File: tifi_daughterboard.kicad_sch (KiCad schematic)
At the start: 23 parts

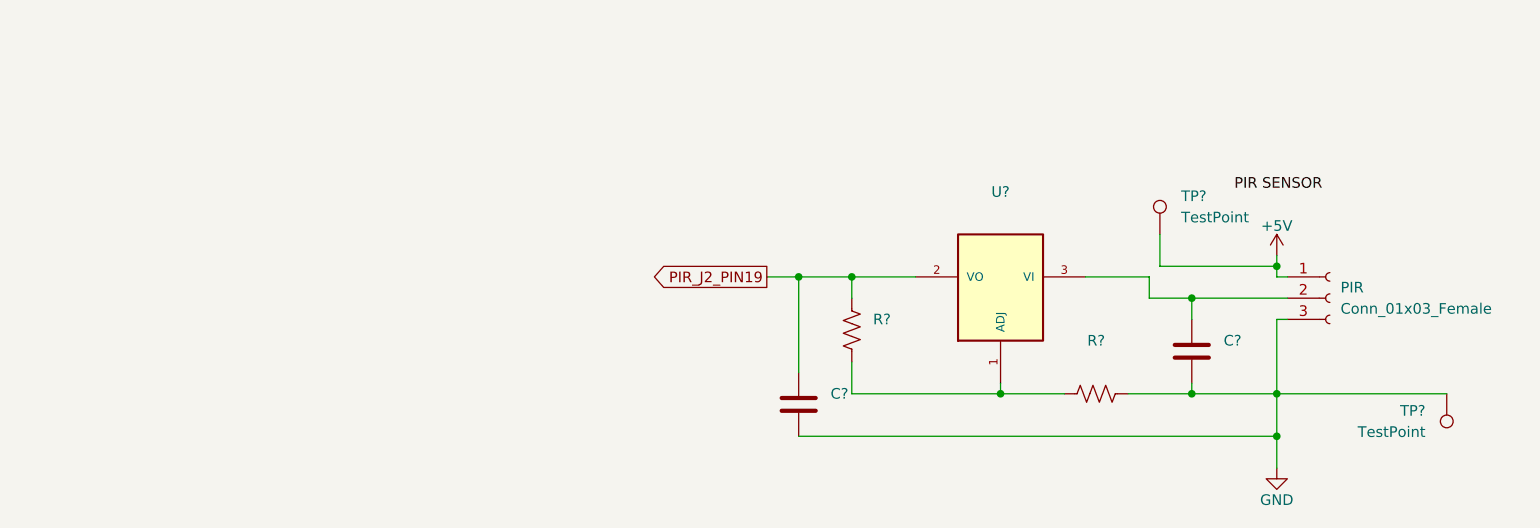
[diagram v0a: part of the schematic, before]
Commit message: Added JST connector for stemma
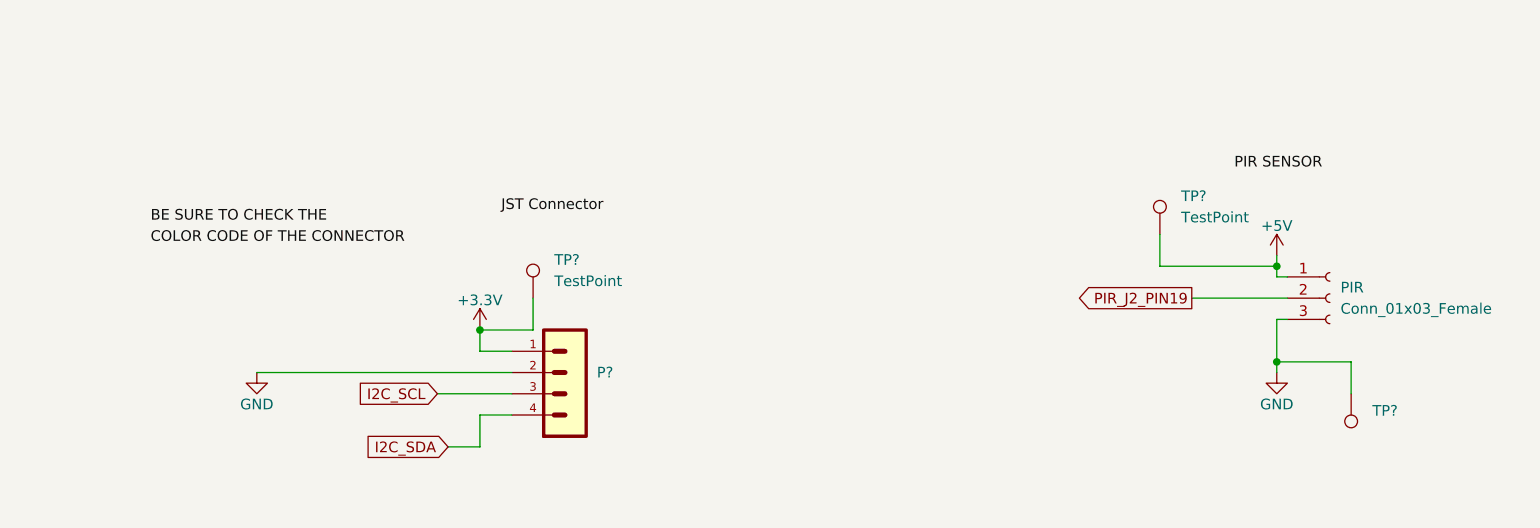
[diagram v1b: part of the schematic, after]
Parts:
- removed C? (x2): (no value), symbol Device:C
- removed R? (x2): (no value), symbol Device:R_US
- removed U?: (no value), symbol LM317:LM317
- added P?: (no value), symbol B4B-PH-K:B4B-PH-K
- added TP?: TestPoint, TestPoint:TestPoint_THTPad_1.0x1.0mm_Drill0.5mm, symbol Connector:TestPoint
- J? (x2): footprint (none) -> Connector_PinHeader_1.00mm:PinHeader_2x10_P1.00mm_Vertical
- LDR: footprint NSL_19M51 -> New Symbols:NSL_19M51
- PIR: footprint (none) -> Connector_PinHeader_1.00mm:PinHeader_1x03_P1.00mm_Vertical
- TP? (x7): footprint (none) -> TestPoint:TestPoint_THTPad_1.0x1.0mm_Drill0.5mm
- TP?: value TestPoint -> (none); footprint (none) -> TestPoint:TestPoint_THTPad_1.0x1.0mm_Drill0.5mm
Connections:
- net +3.3V: now also P?.1, TP?.1
- net GND: now also P?.2
- net I2C_SCL: now also P?.3
- net I2C_SDA: now also P?.4
- net PIR_J2_PIN19: now also PIR.2 (Pin_2)
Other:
- moved on the sheet: TP?

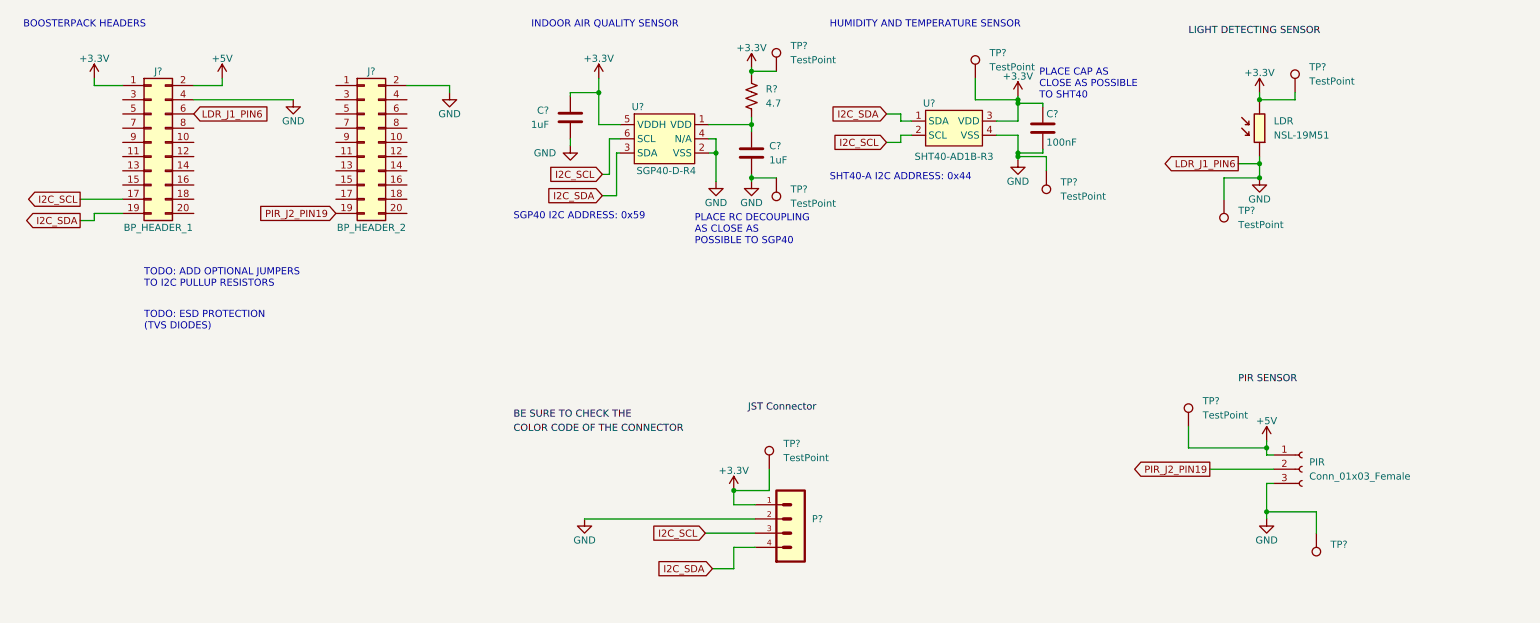
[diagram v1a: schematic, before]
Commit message: Change STEMMA QT connector.
The previous connector had 2mm pitch, changed to 1mm pitch.
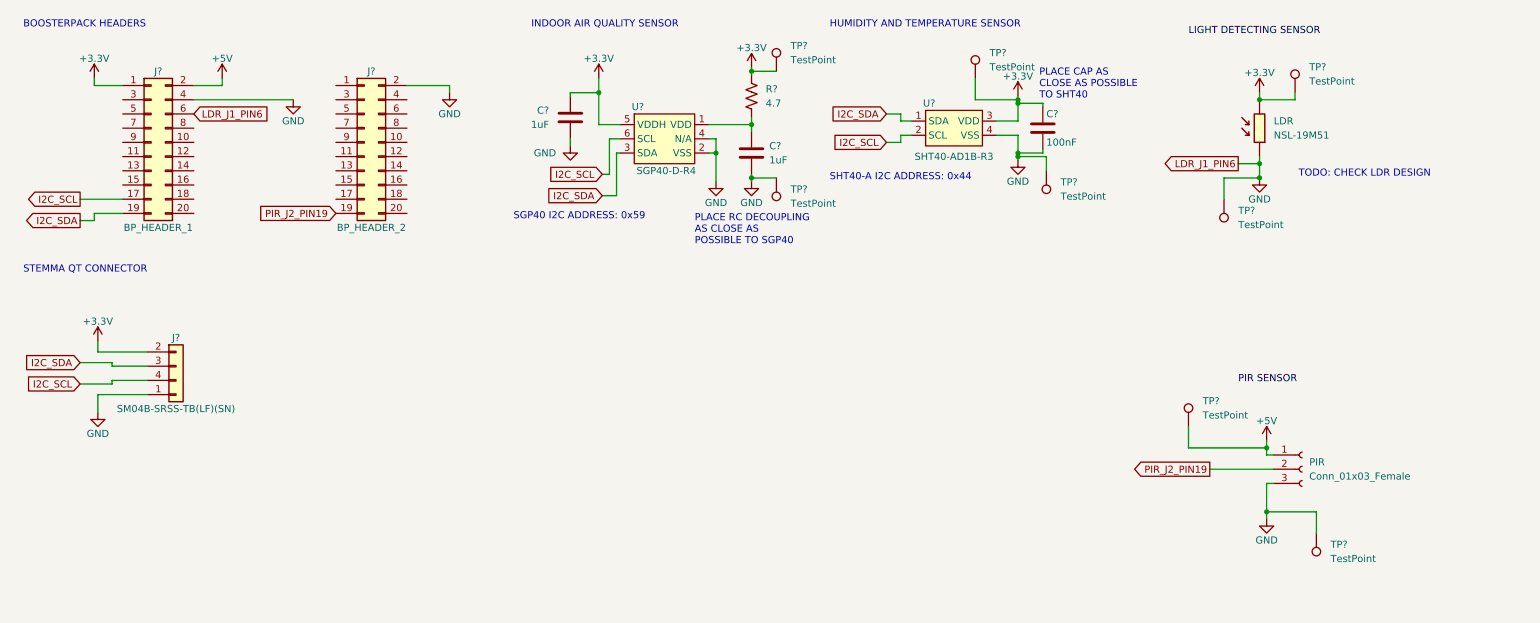
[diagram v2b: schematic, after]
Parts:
- removed P?: (no value), symbol B4B-PH-K:B4B-PH-K
- removed TP?: TestPoint, TestPoint:TestPoint_THTPad_1.0x1.0mm_Drill0.5mm, symbol Connector:TestPoint
- added J?: SM04B-SRSS-TB(LF)(SN), symbol Connector_Generic:Conn_01x04
- TP?: value (none) -> TestPoint
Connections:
- net +3.3V: now also J?.2 (Pin_2)
- net GND: now also J?.1 (Pin_1)
- net I2C_SCL: now also J?.4 (Pin_4)
- net I2C_SDA: now also J?.3 (Pin_3)
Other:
- note added: "STEMMA QT CONNECTOR"
- note added: "TODO: CHECK LDR DESIGN"
- note removed: "TODO: ADD OPTIONAL JUMPERS TO I2C PULLUP RESISTORS"
- note removed: "TODO: ESD PROTECTION (TVS DIODES)"

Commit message: Corrected pitch on BoosterPack headers footprint.
The previous pitch is 1mm, needed to be 2.54mm.
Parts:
- J? (x2): footprint Connector_PinHeader_1.00mm:PinHeader_2x10_P1.00mm_Vertical -> Connector_PinHeader_2.54mm:PinHeader_2x10_P2.54mm_Vertical
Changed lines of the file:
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@@
     (property "Reference" "J?" (id 0) (at 81.28 27.94 0))
     (property "Value" "BP_HEADER_2" (id 1) (at 81.28 55.88 0))
-    (property "Footprint" "Connector_PinHeader_1.00mm:PinHeader_2x10_P1.00mm_Vertical" (id 2) (at 80.01 40.64 0)
+    (property "Footprint" "Connector_PinHeader_2.54mm:PinHeader_2x10_P2.54mm_Vertical" (id 2) (at 80.01 40.64 0)
       (effects (font (size 1.27 1.27)) hide)
     )
@@
   (symbol (lib_id "power:+3.3V") (at 32.385 76.2 0) (unit 1)
     (in_bom yes) (on_board yes)
-    (property "Reference" "#PWR?" (id 0) (at 32.385 80.01 0)
+    (property "Reference" "#PWR0117" (id 0) (at 32.385 80.01 0)
       (effects (font (size 1.27 1.27)) hide)
     )
@@
     (property "Reference" "J?" (id 0) (at 43.18 27.94 0))
     (property "Value" "BP_HEADER_1" (id 1) (at 43.18 55.88 0))
-    (property "Footprint" "Connector_PinHeader_1.00mm:PinHeader_2x10_P1.00mm_Vertical" (id 2) (at 41.91 40.64 0)
+    (property "Footprint" "Connector_PinHeader_2.54mm:PinHeader_2x10_P2.54mm_Vertical" (id 2) (at 41.91 40.64 0)
       (effects (font (size 1.27 1.27)) hide)
     )
@@
   (symbol (lib_id "power:GND") (at 32.385 88.9 0) (unit 1)
     (in_bom yes) (on_board yes)
-    (property "Reference" "#PWR?" (id 0) (at 32.385 95.25 0)
+    (property "Reference" "#PWR0116" (id 0) (at 32.385 95.25 0)
       (effects (font (size 1.27 1.27)) hide)
     )
@@
       (reference "#PWR0115") (unit 1) (value "GND") (footprint "")
     )
+    (path "/fef7b405-bcca-4f18-8c18-a8e7a2c24140"
+      (reference "#PWR0116") (unit 1) (value "GND") (footprint "")
+    )
     (path "/5be1ee84-24e6-4a1e-a679-030b25f95ea3"
-      (reference "#PWR?") (unit 1) (value "+3.3V") (footprint "")
-    )
-    (path "/fef7b405-bcca-4f18-8c18-a8e7a2c24140"
-      (reference "#PWR?") (unit 1) (value "GND") (footprint "")
+      (reference "#PWR0117") (unit 1) (value "+3.3V") (footprint "")
     )
     (path "/2c04621a-bbf8-472b-bd15-1b74530f6f21"
@@
     )
     (path "/03e73a6c-6a66-4743-9386-abd83f09d2a2"
-      (reference "J?") (unit 1) (value "BP_HEADER_2") (footprint "Connector_PinHeader_1.00mm:PinHeader_2x10_P1.00mm_Vertical")
+      (reference "J?") (unit 1) (value "BP_HEADER_2") (footprint "Connector_PinHeader_2.54mm:PinHeader_2x10_P2.54mm_Vertical")
     )
     (path "/7b912d29-33dd-4ac7-bc62-fbbca0b985f1"
@@
     )
     (path "/eec51399-1c9c-497c-8d0a-e34cae999a37"
-      (reference "J?") (unit 1) (value "BP_HEADER_1") (footprint "Connector_PinHeader_1.00mm:PinHeader_2x10_P1.00mm_Vertical")
+      (reference "J?") (unit 1) (value "BP_HEADER_1") (footprint "Connector_PinHeader_2.54mm:PinHeader_2x10_P2.54mm_Vertical")
     )
     (path "/6e3170e0-2cfe-409f-b8c1-c7618fd99f0e"

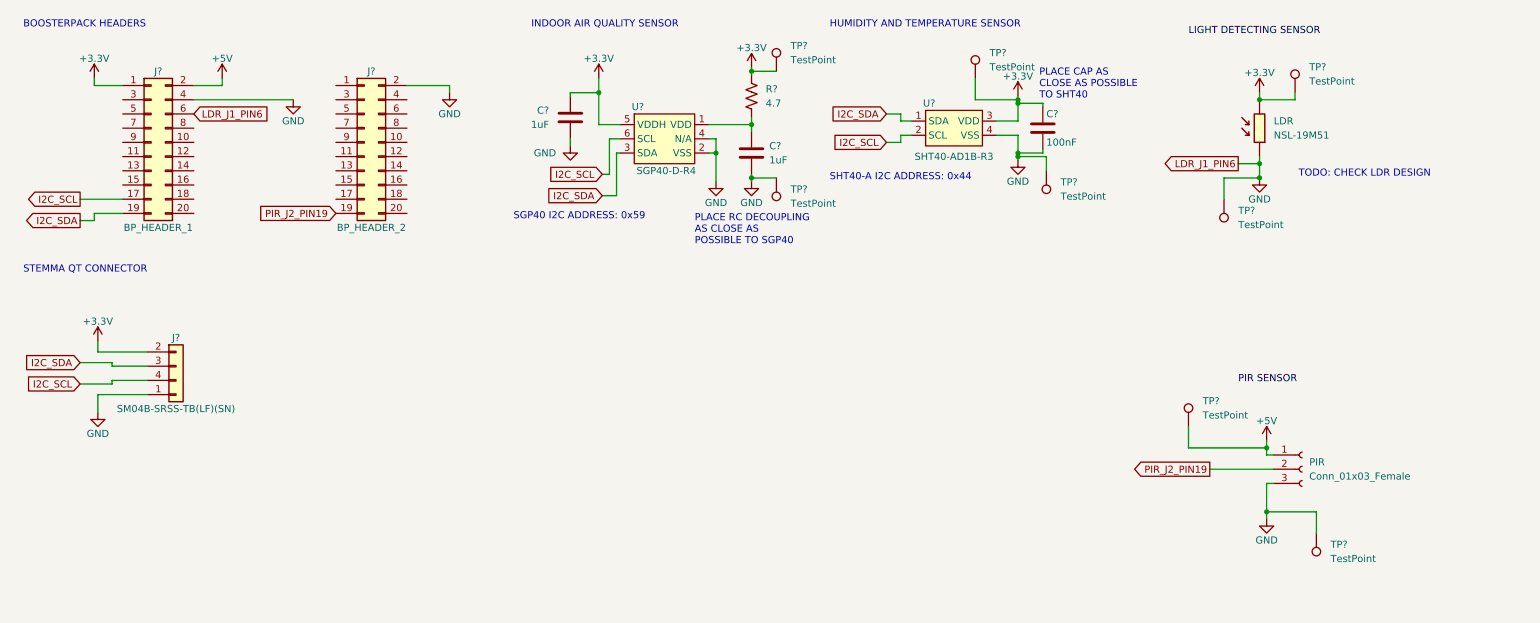
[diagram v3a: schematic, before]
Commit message: Update PIR sensor connector.
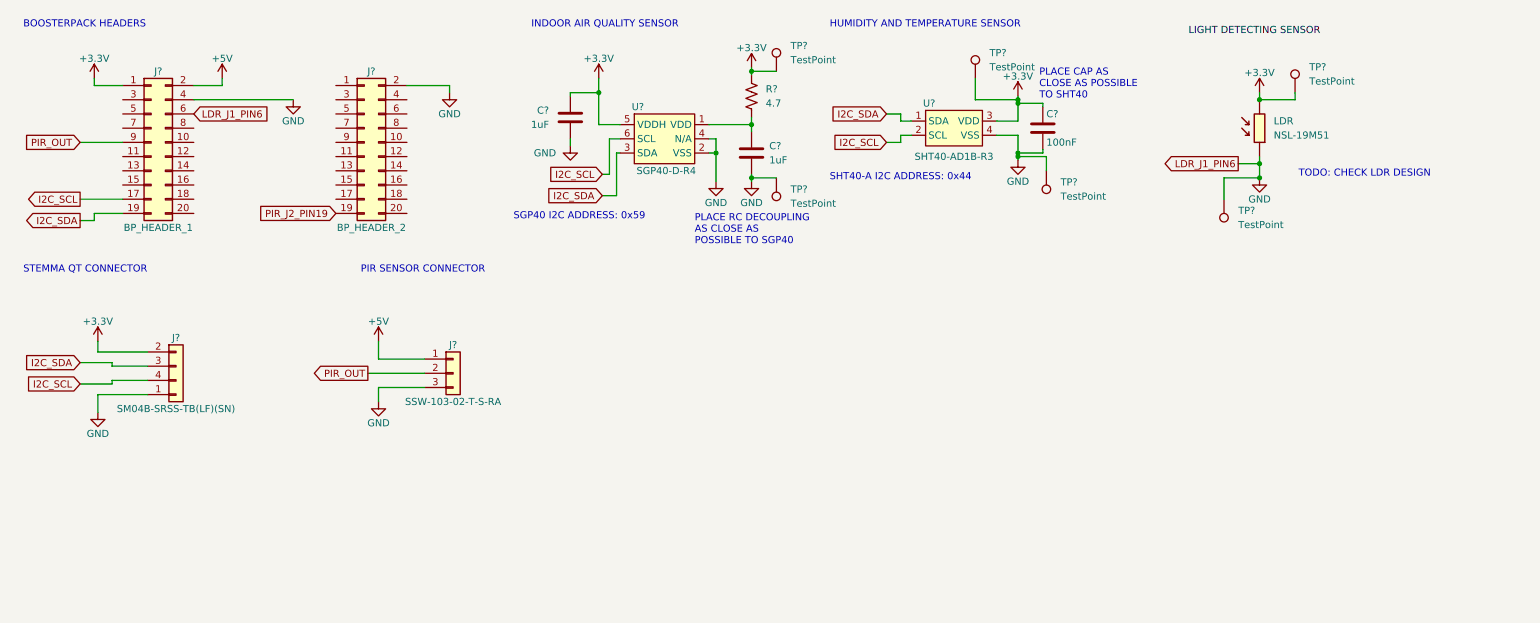
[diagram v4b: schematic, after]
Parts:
- removed PIR: Conn_01x03_Female, Connector_PinHeader_1.00mm:PinHeader_1x03_P1.00mm_Vertical, symbol Connector:Conn_01x03_Female
- removed TP? (x2): TestPoint, TestPoint:TestPoint_THTPad_1.0x1.0mm_Drill0.5mm, symbol Connector:TestPoint
- added J?: SSW-103-02-T-S-RA, Connector_PinSocket_2.54mm:PinSocket_1x03_P2.54mm_Horizontal, symbol Connector_Generic:Conn_01x03
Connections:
- net +5V: now also J?.1 (Pin_1)
- net GND: now also J?.3 (Pin_3)
- net PIR_OUT: now reaches J?.9 (Pin_9)
- net PIR_OUT: now also J?.2 (Pin_2)
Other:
- note added: "PIR SENSOR CONNECTOR"

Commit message: Increase section labels to 70 mils.
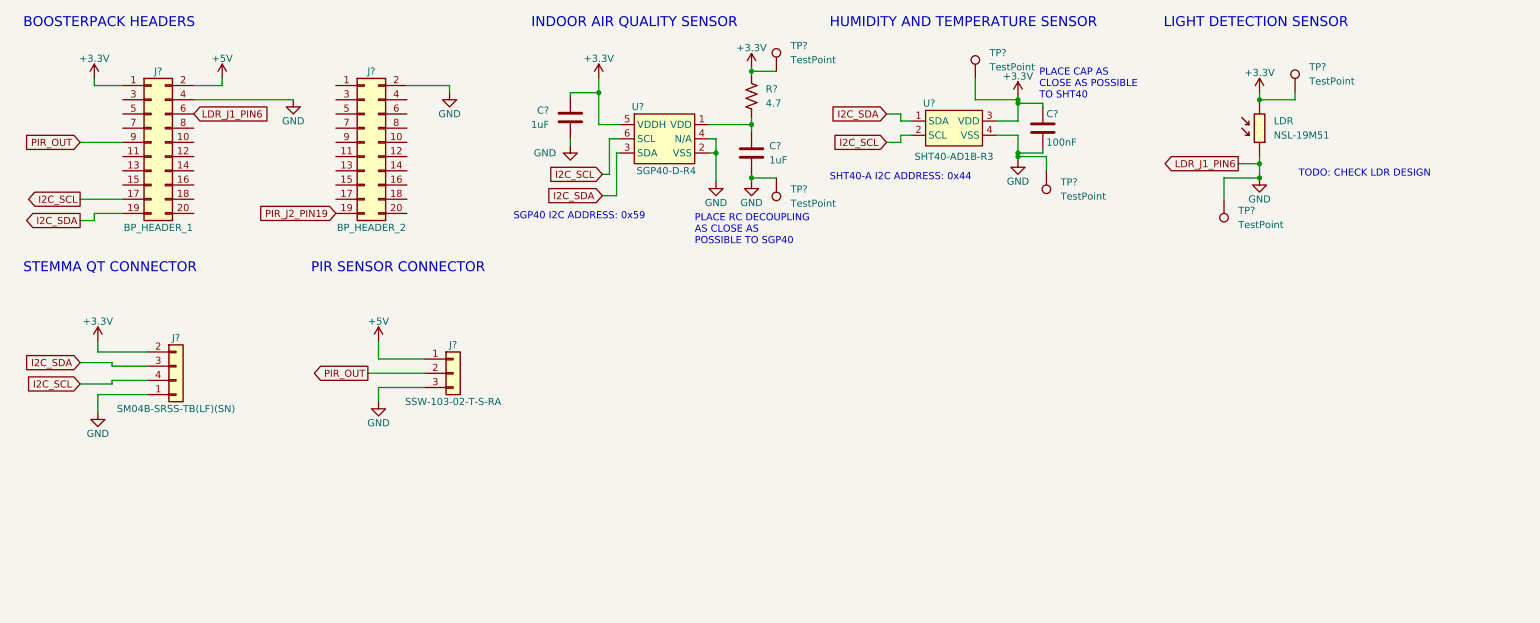
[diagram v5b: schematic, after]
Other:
- note added: "LIGHT DETECTION SENSOR"
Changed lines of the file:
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@@
     (effects (font (size 1.27 1.27)) (justify left bottom))
   )
-  (text "PIR SENSOR CONNECTOR" (at 79.375 64.135 0)
-    (effects (font (size 1.27 1.27)) (justify left bottom))
+  (text "LIGHT DETECTION SENSOR" (at 222.885 20.32 0)
+    (effects (font (size 1.778 1.778)) (justify left bottom))
+  )
+  (text "PIR SENSOR CONNECTOR" (at 70.485 64.135 0)
+    (effects (font (size 1.778 1.778)) (justify left bottom))
   )
   (text "STEMMA QT CONNECTOR" (at 19.05 64.135 0)
-    (effects (font (size 1.27 1.27)) (justify left bottom))
+    (effects (font (size 1.778 1.778)) (justify left bottom))
   )
   (text "HUMIDITY AND TEMPERATURE SENSOR" (at 163.195 20.32 0)
-    (effects (font (size 1.27 1.27)) (justify left bottom))
+    (effects (font (size 1.778 1.778)) (justify left bottom))
   )
   (text "INDOOR AIR QUALITY SENSOR" (at 109.855 20.32 0)
-    (effects (font (size 1.27 1.27)) (justify left bottom))
+    (effects (font (size 1.778 1.778)) (justify left bottom))
   )
   (text "BOOSTERPACK HEADERS" (at 19.05 20.32 0)
-    (effects (font (size 1.27 1.27)) (justify left bottom))
-  )
-  (label "LIGHT DETECTING SENSOR" (at 227.33 21.59 0)
-    (effects (font (size 1.27 1.27)) (justify left bottom))
+    (effects (font (size 1.778 1.778)) (justify left bottom))
   )
   (global_label "I2C_SCL" (shape input) (at 122.555 46.355 180) (fields_autoplaced)
